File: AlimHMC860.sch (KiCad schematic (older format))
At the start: 23 parts, among them U2 HMC860LP3E

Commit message: passage 0402 => 0603
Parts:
- C19: footprint Capacitor_SMD:C_0603_1608Metric -> Capacitor_SMD:C_0603_1608Metric_Pad1.08x0.95mm_HandSolder
- C20, C32, C35, C38: footprint Capacitor_SMD:C_0805_2012Metric -> Capacitor_SMD:C_0603_1608Metric_Pad1.08x0.95mm_HandSolder
- C24, C26, C27, C33, C34, C36, C37: footprint Capacitor_SMD:C_0402_1005Metric -> Capacitor_SMD:C_0603_1608Metric_Pad1.08x0.95mm_HandSolder
- R27, R28, R29, R30, R35, R36, R37, R38, R39, R50: footprint Resistor_SMD:R_0402_1005Metric -> Resistor_SMD:R_0603_1608Metric_Pad0.98x0.95mm_HandSolder
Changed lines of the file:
@@
 F 0 "C34" H 9615 2296 50  0000 L CNN
 F 1 "100n" H 9615 2205 50  0000 L CNN
-F 2 "Capacitor_SMD:C_0402_1005Metric" H 9538 2100 50  0001 C CNN
+F 2 "Capacitor_SMD:C_0603_1608Metric_Pad1.08x0.95mm_HandSolder" H 9538 2100 50  0001 C CNN
 F 3 "~" H 9500 2250 50  0001 C CNN
 	1    9500 2250
@@
 F 0 "C32" H 9115 2296 50  0000 L CNN
 F 1 "10u" H 9115 2205 50  0000 L CNN
-F 2 "Capacitor_SMD:C_0805_2012Metric" H 9038 2100 50  0001 C CNN
+F 2 "Capacitor_SMD:C_0603_1608Metric_Pad1.08x0.95mm_HandSolder" H 9038 2100 50  0001 C CNN
 F 3 "~" H 9000 2250 50  0001 C CNN
 	1    9000 2250
@@
 F 0 "C20" H 2615 3296 50  0000 L CNN
 F 1 "4.7u" H 2615 3205 50  0000 L CNN
-F 2 "Capacitor_SMD:C_0805_2012Metric" H 2538 3100 50  0001 C CNN
+F 2 "Capacitor_SMD:C_0603_1608Metric_Pad1.08x0.95mm_HandSolder" H 2538 3100 50  0001 C CNN
 F 3 "~" H 2500 3250 50  0001 C CNN
 	1    2500 3250
@@
 F 0 "R29" V 6900 2000 50  0000 C CNN
 F 1 "0.2" V 7000 2000 50  0000 C CNN
-F 2 "Resistor_SMD:R_0402_1005Metric" V 6930 2000 50  0001 C CNN
+F 2 "Resistor_SMD:R_0603_1608Metric_Pad0.98x0.95mm_HandSolder" V 6930 2000 50  0001 C CNN
 F 3 "~" H 7000 2000 50  0001 C CNN
 	1    7000 2000
@@
 F 0 "R30" V 7543 3000 50  0000 C CNN
 F 1 "1k" V 7634 3000 50  0000 C CNN
-F 2 "Resistor_SMD:R_0402_1005Metric" V 7680 3000 50  0001 C CNN
+F 2 "Resistor_SMD:R_0603_1608Metric_Pad0.98x0.95mm_HandSolder" V 7680 3000 50  0001 C CNN
 F 3 "~" H 7750 3000 50  0001 C CNN
 	1    7750 3000
@@
 F 0 "R28" V 9150 3000 50  0000 C CNN
 F 1 "0" V 9250 3000 50  0000 C CNN
-F 2 "Resistor_SMD:R_0402_1005Metric" V 9180 3000 50  0001 C CNN
+F 2 "Resistor_SMD:R_0603_1608Metric_Pad0.98x0.95mm_HandSolder" V 9180 3000 50  0001 C CNN
 F 3 "~" H 9250 3000 50  0001 C CNN
 	1    9250 3000
@@
 F 0 "R39" V 9043 3500 50  0000 C CNN
 F 1 "DEPOP" V 9134 3500 50  0000 C CNN
-F 2 "Resistor_SMD:R_0402_1005Metric" V 9180 3500 50  0001 C CNN
+F 2 "Resistor_SMD:R_0603_1608Metric_Pad0.98x0.95mm_HandSolder" V 9180 3500 50  0001 C CNN
 F 3 "~" H 9250 3500 50  0001 C CNN
 	1    9250 3500
@@
 F 0 "C37" H 9615 4796 50  0000 L CNN
 F 1 "100n" H 9615 4705 50  0000 L CNN
-F 2 "Capacitor_SMD:C_0402_1005Metric" H 9538 4600 50  0001 C CNN
+F 2 "Capacitor_SMD:C_0603_1608Metric_Pad1.08x0.95mm_HandSolder" H 9538 4600 50  0001 C CNN
 F 3 "~" H 9500 4750 50  0001 C CNN
 	1    9500 4750
@@
 F 0 "C38" H 9115 4796 50  0000 L CNN
 F 1 "10u" H 9115 4705 50  0000 L CNN
-F 2 "Capacitor_SMD:C_0805_2012Metric" H 9038 4600 50  0001 C CNN
+F 2 "Capacitor_SMD:C_0603_1608Metric_Pad1.08x0.95mm_HandSolder" H 9038 4600 50  0001 C CNN
 F 3 "~" H 9000 4750 50  0001 C CNN
 	1    9000 4750
@@
 F 0 "C19" H 4115 3596 50  0000 L CNN
 F 1 "1u" H 4115 3505 50  0000 L CNN
-F 2 "Capacitor_SMD:C_0603_1608Metric" H 4038 3400 50  0001 C CNN
+F 2 "Capacitor_SMD:C_0603_1608Metric_Pad1.08x0.95mm_HandSolder" H 4038 3400 50  0001 C CNN
 F 3 "~" H 4000 3550 50  0001 C CNN
 	1    4000 3550
@@
 F 0 "C26" V 6100 4000 50  0000 C CNN
 F 1 "100n" V 6400 4000 50  0000 C CNN
-F 2 "Capacitor_SMD:C_0402_1005Metric" H 6288 3850 50  0001 C CNN
+F 2 "Capacitor_SMD:C_0603_1608Metric_Pad1.08x0.95mm_HandSolder" H 6288 3850 50  0001 C CNN
 F 3 "~" H 6250 4000 50  0001 C CNN
 	1    6250 4000
@@
 F 0 "C27" V 4998 2000 50  0000 C CNN
 F 1 "100n" V 5089 2000 50  0000 C CNN
-F 2 "Capacitor_SMD:C_0402_1005Metric" H 5288 1850 50  0001 C CNN
+F 2 "Capacitor_SMD:C_0603_1608Metric_Pad1.08x0.95mm_HandSolder" H 5288 1850 50  0001 C CNN
 F 3 "~" H 5250 2000 50  0001 C CNN
 	1    5250 2000
@@
 F 0 "R38" V 7543 3500 50  0000 C CNN
 F 1 "1k" V 7634 3500 50  0000 C CNN
-F 2 "Resistor_SMD:R_0402_1005Metric" V 7680 3500 50  0001 C CNN
+F 2 "Resistor_SMD:R_0603_1608Metric_Pad0.98x0.95mm_HandSolder" V 7680 3500 50  0001 C CNN
 F 3 "~" H 7750 3500 50  0001 C CNN
 	1    7750 3500
@@
 F 0 "R50" H 7930 3704 50  0000 R CNN
 F 1 "1k" H 7930 3795 50  0000 R CNN
-F 2 "Resistor_SMD:R_0402_1005Metric" V 7930 3750 50  0001 C CNN
+F 2 "Resistor_SMD:R_0603_1608Metric_Pad0.98x0.95mm_HandSolder" V 7930 3750 50  0001 C CNN
 F 3 "~" H 8000 3750 50  0001 C CNN
 	1    8000 3750
@@
 F 0 "R27" H 8430 3704 50  0000 R CNN
 F 1 "1k" H 8430 3795 50  0000 R CNN
-F 2 "Resistor_SMD:R_0402_1005Metric" V 8430 3750 50  0001 C CNN
+F 2 "Resistor_SMD:R_0603_1608Metric_Pad0.98x0.95mm_HandSolder" V 8430 3750 50  0001 C CNN
 F 3 "~" H 8500 3750 50  0001 C CNN
 	1    8500 3750
@@
 F 0 "R37" V 7150 4500 50  0000 C CNN
 F 1 "0.2" V 7250 4500 50  0000 C CNN
-F 2 "Resistor_SMD:R_0402_1005Metric" V 7180 4500 50  0001 C CNN
+F 2 "Resistor_SMD:R_0603_1608Metric_Pad0.98x0.95mm_HandSolder" V 7180 4500 50  0001 C CNN
 F 3 "~" H 7250 4500 50  0001 C CNN
 	1    7250 4500
@@
 F 0 "R35" H 6650 3350 50  0000 C CNN
 F 1 "1" H 6500 3300 50  0000 C CNN
-F 2 "Resistor_SMD:R_0402_1005Metric" V 6430 3300 50  0001 C CNN
+F 2 "Resistor_SMD:R_0603_1608Metric_Pad0.98x0.95mm_HandSolder" V 6430 3300 50  0001 C CNN
 F 3 "~" H 6500 3300 50  0001 C CNN
 	1    6500 3300
@@
 F 0 "C24" V 5350 5500 50  0000 C CNN
 F 1 "100n" V 5650 5500 50  0000 C CNN
-F 2 "Capacitor_SMD:C_0402_1005Metric" H 5538 5350 50  0001 C CNN
+F 2 "Capacitor_SMD:C_0603_1608Metric_Pad1.08x0.95mm_HandSolder" H 5538 5350 50  0001 C CNN
 F 3 "~" H 5500 5500 50  0001 C CNN
 	1    5500 5500
@@
 F 0 "C36" H 9615 5796 50  0000 L CNN
 F 1 "100n" H 9615 5705 50  0000 L CNN
-F 2 "Capacitor_SMD:C_0402_1005Metric" H 9538 5600 50  0001 C CNN
+F 2 "Capacitor_SMD:C_0603_1608Metric_Pad1.08x0.95mm_HandSolder" H 9538 5600 50  0001 C CNN
 F 3 "~" H 9500 5750 50  0001 C CNN
 	1    9500 5750
@@
 F 0 "C35" H 9115 5796 50  0000 L CNN
 F 1 "10u" H 9115 5705 50  0000 L CNN
-F 2 "Capacitor_SMD:C_0805_2012Metric" H 9038 5600 50  0001 C CNN
+F 2 "Capacitor_SMD:C_0603_1608Metric_Pad1.08x0.95mm_HandSolder" H 9038 5600 50  0001 C CNN
 F 3 "~" H 9000 5750 50  0001 C CNN
 	1    9000 5750
@@
 F 0 "R36" V 8650 5500 50  0000 C CNN
 F 1 "0.2" V 8750 5500 50  0000 C CNN
-F 2 "Resistor_SMD:R_0402_1005Metric" V 8680 5500 50  0001 C CNN
+F 2 "Resistor_SMD:R_0603_1608Metric_Pad0.98x0.95mm_HandSolder" V 8680 5500 50  0001 C CNN
 F 3 "~" H 8750 5500 50  0001 C CNN
 	1    8750 5500
@@
 F 0 "C33" H 7115 2796 50  0000 L CNN
 F 1 "100n" H 7115 2705 50  0000 L CNN
-F 2 "Capacitor_SMD:C_0402_1005Metric" H 7038 2600 50  0001 C CNN
+F 2 "Capacitor_SMD:C_0603_1608Metric_Pad1.08x0.95mm_HandSolder" H 7038 2600 50  0001 C CNN
 F 3 "~" H 7000 2750 50  0001 C CNN
 	1    7000 2750

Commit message: v0 Routing done
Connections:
- net IO_SUPPLY: no longer names the net of C35.1, C36.1, R36.1
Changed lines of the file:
@@
 $EndComp
-Wire Wire Line
-	9500 5500 9600 5500
 Wire Wire Line
 	9500 1900 9500 2000
@@
 Wire Wire Line
 	9500 4500 9600 4500
-Text GLabel 9600 5500 2    50   Input ~ 0
-IO_SUPPLY
 $EndSCHEMATC

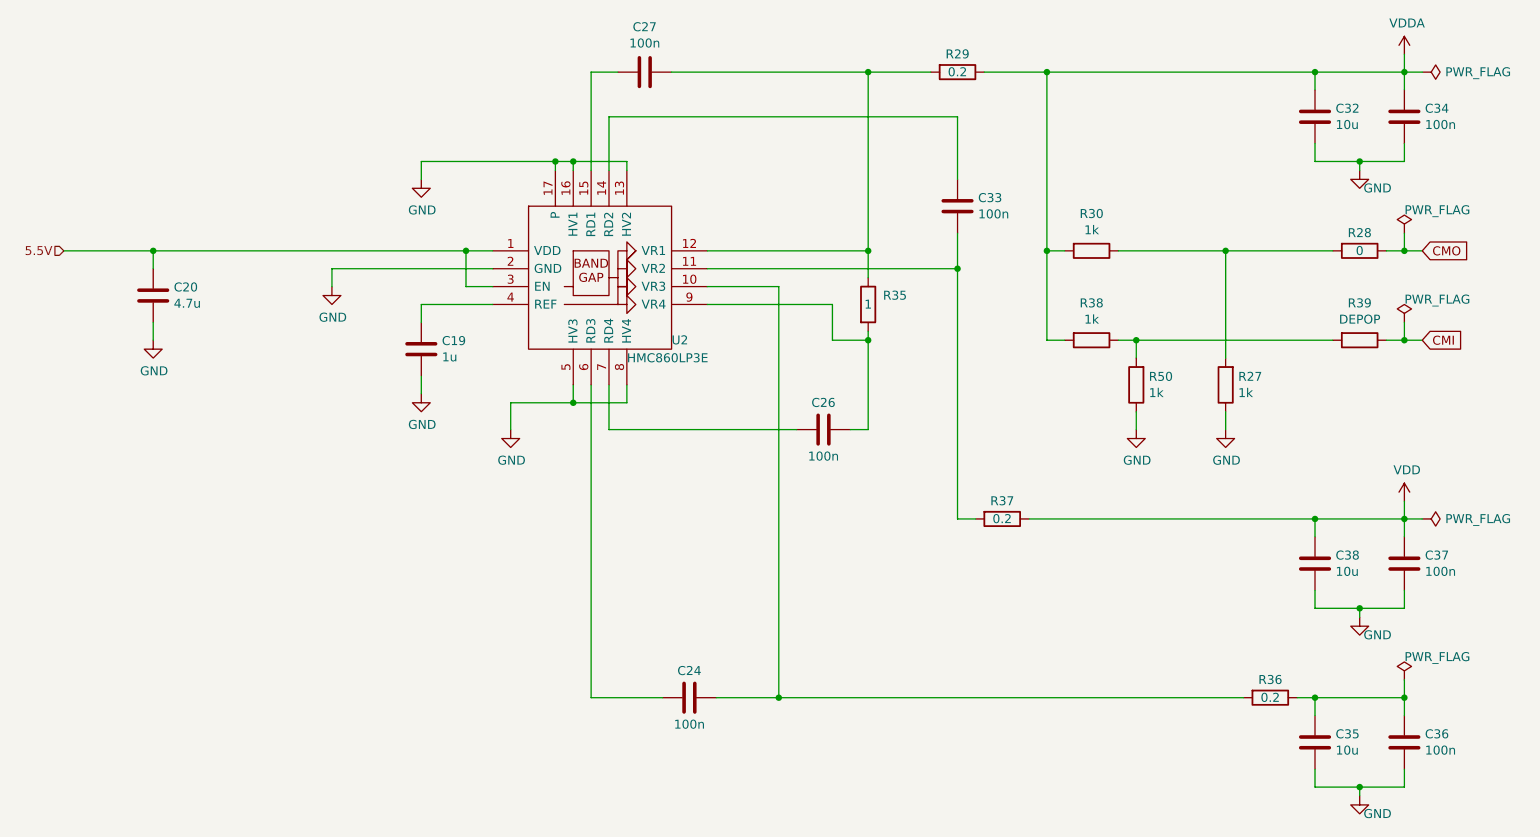
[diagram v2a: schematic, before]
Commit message: reorganized to match power consumption
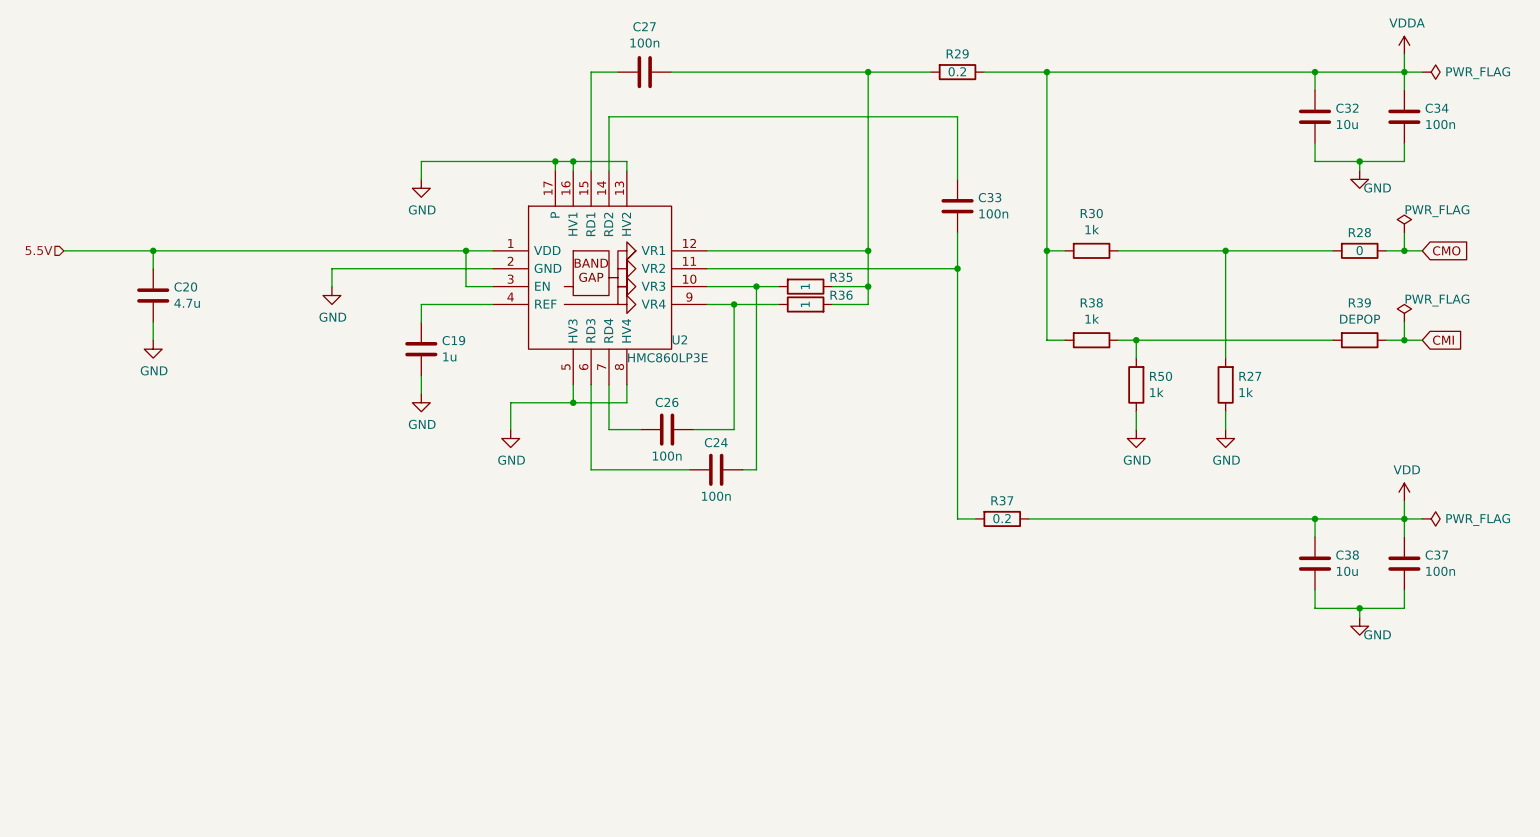
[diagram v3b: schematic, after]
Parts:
- removed C35: 10u, Capacitor_SMD:C_0603_1608Metric_Pad1.08x0.95mm_HandSolder, symbol Device:C
- removed C36: 100n, Capacitor_SMD:C_0603_1608Metric_Pad1.08x0.95mm_HandSolder, symbol Device:C
- R36: value 0.2 -> 1
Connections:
- net at C27.1, R29.2, U2.12 (VR1): now also R35.2, R36.1; no longer R35.1
- net at C26.1, U2.9 (VR4): now also R35.1; no longer R35.2
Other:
- moved on the sheet: C24, C26, R35
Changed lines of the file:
@@
 L Device:C C?
 U 1 1 618A0679
-P 6250 4000
+P 5375 4000
 AR Path="/618A0679" Ref="C?"  Part="1"
 AR Path="/6188E6DD/618A0679" Ref="C26"  Part="1"
-F 0 "C26" V 6100 4000 50  0000 C CNN
-F 1 "100n" V 6400 4000 50  0000 C CNN
-F 2 "Capacitor_SMD:C_0603_1608Metric_Pad1.08x0.95mm_HandSolder" H 6288 3850 50  0001 C CNN
-F 3 "~" H 6250 4000 50  0001 C CNN
-	1    6250 4000
-	0    1    1    0
-$EndComp
-Wire Wire Line
-	6400 4000 6500 4000
+F 0 "C26" V 5225 4000 50  0000 C CNN
+F 1 "100n" V 5525 4000 50  0000 C CNN
+F 2 "Capacitor_SMD:C_0603_1608Metric_Pad1.08x0.95mm_HandSolder" H 5413 3850 50  0001 C CNN
+F 3 "~" H 5375 4000 50  0001 C CNN
+	1    5375 4000
+	0    1    1    0
+$EndComp
+Wire Wire Line
+	5525 4000 5750 4000
 $Comp
 L Device:C C?
@@
 $EndComp
 $Comp
-L Device:R R?
-U 1 1 618E73CC
-P 6500 3300
-AR Path="/618E73CC" Ref="R?"  Part="1"
-AR Path="/6188E6DD/618E73CC" Ref="R35"  Part="1"
-F 0 "R35" H 6650 3350 50  0000 C CNN
-F 1 "1" H 6500 3300 50  0000 C CNN
-F 2 "Resistor_SMD:R_0603_1608Metric_Pad0.98x0.95mm_HandSolder" V 6430 3300 50  0001 C CNN
-F 3 "~" H 6500 3300 50  0001 C CNN
-	1    6500 3300
-	1    0    0    -1
-$EndComp
-$Comp
 L Device:C C?
 U 1 1 618FCC1B
-P 5500 5500
+P 5650 4225
 AR Path="/618FCC1B" Ref="C?"  Part="1"
 AR Path="/6188E6DD/618FCC1B" Ref="C24"  Part="1"
-F 0 "C24" V 5350 5500 50  0000 C CNN
-F 1 "100n" V 5650 5500 50  0000 C CNN
-F 2 "Capacitor_SMD:C_0603_1608Metric_Pad1.08x0.95mm_HandSolder" H 5538 5350 50  0001 C CNN
-F 3 "~" H 5500 5500 50  0001 C CNN
-	1    5500 5500
+F 0 "C24" V 5500 4225 50  0000 C CNN
+F 1 "100n" V 5800 4225 50  0000 C CNN
+F 2 "Capacitor_SMD:C_0603_1608Metric_Pad1.08x0.95mm_HandSolder" H 5688 4075 50  0001 C CNN
+F 3 "~" H 5650 4225 50  0001 C CNN
+	1    5650 4225
 	0    1    1    0
 $EndComp
@@
 Wire Wire Line
 	8500 3900 8500 4000
-$Comp
-L Device:C C?
-U 1 1 6191B932
-P 9500 5750
-AR Path="/6191B932" Ref="C?"  Part="1"
-AR Path="/6188E6DD/6191B932" Ref="C36"  Part="1"
-F 0 "C36" H 9615 5796 50  0000 L CNN
-F 1 "100n" H 9615 5705 50  0000 L CNN
-F 2 "Capacitor_SMD:C_0603_1608Metric_Pad1.08x0.95mm_HandSolder" H 9538 5600 50  0001 C CNN
-F 3 "~" H 9500 5750 50  0001 C CNN
-	1    9500 5750
-	1    0    0    -1
-$EndComp
-$Comp
-L Device:C C?
-U 1 1 6191BAAC
-P 9000 5750
-AR Path="/6191BAAC" Ref="C?"  Part="1"
-AR Path="/6188E6DD/6191BAAC" Ref="C35"  Part="1"
-F 0 "C35" H 9115 5796 50  0000 L CNN
-F 1 "10u" H 9115 5705 50  0000 L CNN
-F 2 "Capacitor_SMD:C_0603_1608Metric_Pad1.08x0.95mm_HandSolder" H 9038 5600 50  0001 C CNN
-F 3 "~" H 9000 5750 50  0001 C CNN
-	1    9000 5750
-	1    0    0    -1
-$EndComp
-Wire Wire Line
-	9000 5600 9000 5500
-Wire Wire Line
-	9000 5500 9500 5500
-Wire Wire Line
-	9500 5500 9500 5600
-Wire Wire Line
-	9500 5900 9500 6000
-Wire Wire Line
-	9500 6000 9250 6000
-Wire Wire Line
-	9000 6000 9000 5900
-$Comp
-L power:GND #PWR?
-U 1 1 6191BABC
-P 9250 6050
-AR Path="/60D21B6E/6191BABC" Ref="#PWR?"  Part="1"
-AR Path="/6191BABC" Ref="#PWR?"  Part="1"
-AR Path="/6188E6DD/6191BABC" Ref="#PWR0151"  Part="1"
-F 0 "#PWR0151" H 9250 5800 50  0001 C CNN
-F 1 "GND" H 9350 5950 50  0000 C CNN
-F 2 "" H 9250 6050 50  0001 C CNN
-F 3 "" H 9250 6050 50  0001 C CNN
-	1    9250 6050
-	1    0    0    -1
-$EndComp
-Wire Wire Line
-	9250 6000 9250 6050
-Connection ~ 9250 6000
-Wire Wire Line
-	9250 6000 9000 6000
-$Comp
-L Device:R R?
-U 1 1 61935C1F
-P 8750 5500
-AR Path="/61935C1F" Ref="R?"  Part="1"
-AR Path="/6188E6DD/61935C1F" Ref="R36"  Part="1"
-F 0 "R36" V 8650 5500 50  0000 C CNN
-F 1 "0.2" V 8750 5500 50  0000 C CNN
-F 2 "Resistor_SMD:R_0603_1608Metric_Pad0.98x0.95mm_HandSolder" V 8680 5500 50  0001 C CNN
-F 3 "~" H 8750 5500 50  0001 C CNN
-	1    8750 5500
-	0    1    1    0
-$EndComp
-Wire Wire Line
-	5650 5500 6000 5500
-Wire Wire Line
-	8900 5500 9000 5500
-Connection ~ 9000 5500
-Connection ~ 6000 5500
-Wire Wire Line
-	6000 5500 8600 5500
+Wire Wire Line
+	5800 4225 5875 4225
 Wire Wire Line
 	9000 4500 7400 4500
@@
 	5600 3000 6500 3000
 Wire Wire Line
-	6500 3000 6500 3150
-Wire Wire Line
-	5600 3300 6300 3300
-Wire Wire Line
-	6300 3300 6300 3500
-Wire Wire Line
-	6300 3500 6500 3500
-Wire Wire Line
-	6500 3500 6500 3450
-Wire Wire Line
-	6500 3500 6500 4000
-Connection ~ 6500 3500
+	6500 3000 6500 3200
 Wire Wire Line
 	5050 4000 5050 3750
 Wire Wire Line
-	5050 4000 6100 4000
-Wire Wire Line
-	6000 3200 5600 3200
-Wire Wire Line
-	6000 3200 6000 5500
-Wire Wire Line
-	4950 3750 4950 5500
-Wire Wire Line
-	4950 5500 5350 5500
+	5050 4000 5225 4000
+Wire Wire Line
+	6000 3200 5875 3200
+Wire Wire Line
+	4950 3750 4950 4225
+Wire Wire Line
+	4950 4225 5500 4225
 Wire Wire Line
 	4950 2550 4950 2000
@@
 	1    0    0    -1
 $EndComp
-Wire Wire Line
-	9500 5400 9500 5500
-Connection ~ 9500 5500
 Connection ~ 9500 2000
 $Comp
@@
 Wire Wire Line
 	9500 3500 9600 3500
-$Comp
-L power:PWR_FLAG #FLG0105
-U 1 1 61A30FDA
-P 9500 5400
-F 0 "#FLG0105" H 9500 5475 50  0001 C CNN
-F 1 "PWR_FLAG" H 9500 5528 50  0000 L CNN
-F 2 "" H 9500 5400 50  0001 C CNN
-F 3 "~" H 9500 5400 50  0001 C CNN
-	1    9500 5400
-	1    0    0    -1
-$EndComp
 Wire Wire Line
 	9500 1900 9500 2000
@@
 Wire Wire Line
 	9500 4500 9600 4500
+Wire Wire Line
+	5750 3300 5750 4000
+$Comp
+L Device:R R?
+U 1 1 6113FA14
+P 6150 3200
+AR Path="/6113FA14" Ref="R?"  Part="1"
+AR Path="/6188E6DD/6113FA14" Ref="R36"  Part="1"
+F 0 "R36" V 6200 3400 50  0000 C CNN
+F 1 "1" H 6150 3200 50  0000 C CNN
+F 2 "Resistor_SMD:R_0603_1608Metric_Pad0.98x0.95mm_HandSolder" V 6080 3200 50  0001 C CNN
+F 3 "~" H 6150 3200 50  0001 C CNN
+	1    6150 3200
+	0    1    1    0
+$EndComp
+Wire Wire Line
+	5875 4225 5875 3200
+Connection ~ 5875 3200
+Wire Wire Line
+	5875 3200 5600 3200
+Wire Wire Line
+	5600 3300 5750 3300
+Connection ~ 5750 3300
+Wire Wire Line
+	5750 3300 6000 3300
+Wire Wire Line
+	6300 3200 6500 3200
+Wire Wire Line
+	6300 3300 6500 3300
+Wire Wire Line
+	6500 3300 6500 3200
+Connection ~ 6500 3200
+$Comp
+L Device:R R?
+U 1 1 618E73CC
+P 6150 3300
+AR Path="/618E73CC" Ref="R?"  Part="1"
+AR Path="/6188E6DD/618E73CC" Ref="R35"  Part="1"
+F 0 "R35" V 6300 3100 50  0000 C CNN
+F 1 "1" H 6150 3300 50  0000 C CNN
+F 2 "Resistor_SMD:R_0603_1608Metric_Pad0.98x0.95mm_HandSolder" V 6080 3300 50  0001 C CNN
+F 3 "~" H 6150 3300 50  0001 C CNN
+	1    6150 3300
+	0    -1   -1   0
+$EndComp
 $EndSCHEMATC
